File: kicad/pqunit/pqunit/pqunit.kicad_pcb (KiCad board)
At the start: 2 copper layers, 42 x 42 mm, 15 parts, among them J1 Conn_02x10_PQSU, J2 Conn_01x10, U1 ATMEGA328P-AU, U5 MAX485E, U6 Ai-Thinker-Ra-02, Y1 Crystal

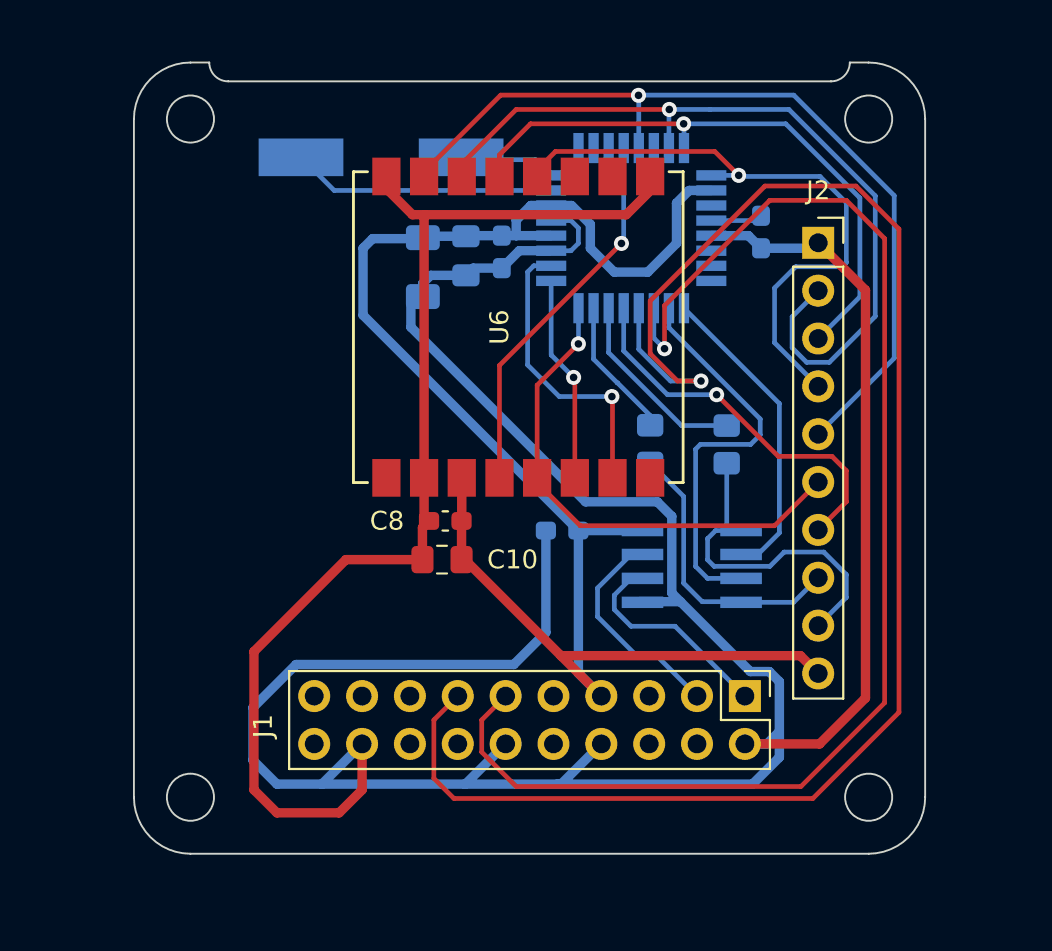
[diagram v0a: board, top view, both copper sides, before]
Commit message: Began PQUnit PCB Rev 2
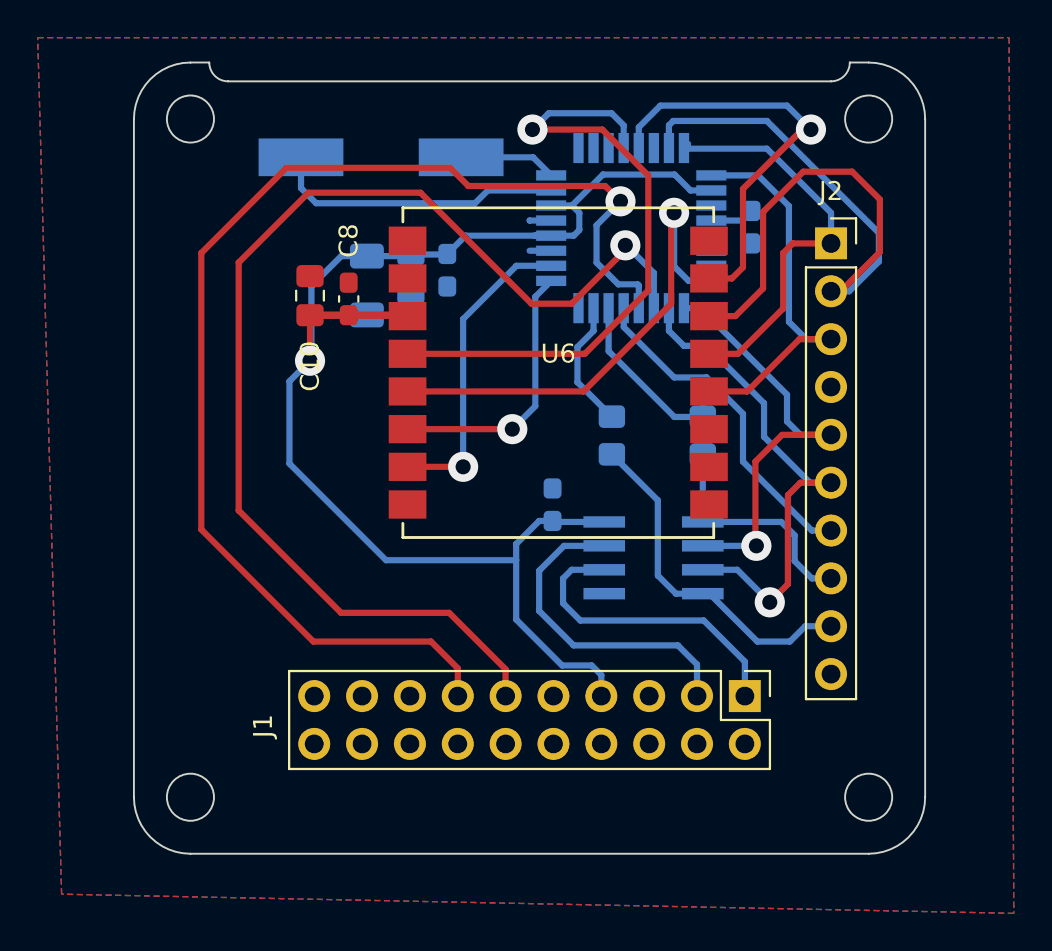
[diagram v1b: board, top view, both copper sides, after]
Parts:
- moved C10 15.7 mm to (131.3, 103.1), turned to 90 degrees
- moved C8 12.9 mm to (133.3, 103.3), turned to 90 degrees
- moved U6 3.21 mm to (144.4, 107.2), turned to 0 degrees
- moved C2 3.13 mm to (134.3, 102.6)
- moved C1 3.08 mm to (136.6, 102.0)
- moved C5 3.05 mm to (138.6, 101.8)
- moved R4 2.08 mm to (147.3, 110.6)
- moved U5 2.08 mm to (149.5, 117.1)
- moved C9 1.46 mm to (144.1, 114.2), turned to 90 degrees
- moved R3 1.35 mm to (152.1, 110.6)
- moved J2 0.68 mm to (158.9, 100.4)
- moved C4 0.56 mm to (154.7, 99.5)
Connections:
- J2 pad 1: GND -> SPI_MISO
- J2 pad 10: +3V3 -> GND
- J2 pad 3: SPI_MISO -> SPI_SCK
- J2 pad 4: SPI_SCK -> GND
- J2 pad 5: RF_NSS -> RS485_NRE
- J2 pad 6: RF_DIO0 -> RS485_DE
- J2 pad 8: MCU_TX -> MCU_RX
- J2 pad 9: MCU_RX -> MCU_TX
- U1 pad 24: unconnected-(U1-PC1(ADC1)-Pad24) -> RF_DIO0
- U1 pad 32: RF_DIO0 -> unconnected-(U1-PD2(INT0)-Pad32)
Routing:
- net GND: track 216.3 -> 2.30 mm
- net RF_NSS: track 46.3 -> 21.5 mm
- net I2C_SCL: track 86.5 -> 65.4 mm
- net +3V3: track 88.3 -> 74.2 mm, vias 0 -> 1
- net RF_NRESET: track 20.2 -> 34.1 mm
- net SPI_SCK: track 33.5 -> 21.8 mm, vias 1 -> 0
- net SPI_MISO: track 32.3 -> 21.8 mm, vias 1 -> 0
- net I2C_SDA: track 71.6 -> 62.2 mm
- net RS485_NRE: track 17.0 -> 23.4 mm, vias 0 -> 1
- net MCU_RX: track 18.4 -> 12.4 mm
- net RS485_SDB: track 11.5 -> 17.4 mm
- net RS485_DE: track 21.4 -> 27.1 mm, vias 0 -> 1
- net RS485_SDA: track 11.7 -> 16.5 mm
- net MCU_TX: track 14.7 -> 18.4 mm
- net RF_DIO1: track 11.0 -> 14.4 mm
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- added copper zone on B.Cu, net GND
- added copper zone on F.Cu, net GND

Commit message: Fixed all PQUnit PCB Rev 2 errors
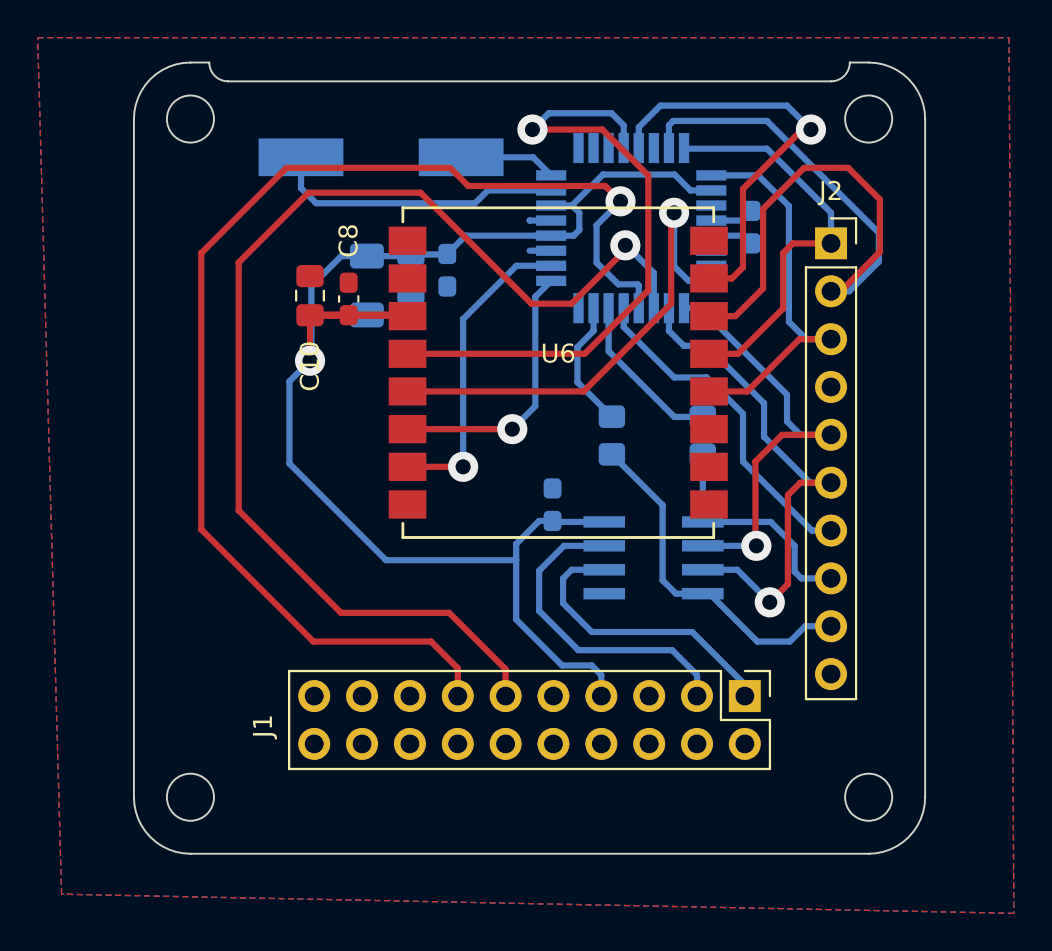
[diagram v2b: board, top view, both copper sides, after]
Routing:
- net GND: track 2.30 -> 4.61 mm
- net RS485_SDA: track 16.5 -> 15.7 mm
- net SPI_SCK: track 21.8 -> 21.2 mm
- net Net-(U1-PD0(RXD)): track 9.35 -> 8.73 mm

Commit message: Finished both PCB latest revisions
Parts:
- added JP1: Jumper_2_Bridged, TestPoint:TestPoint_2Pads_Pitch2.54mm_Drill0.8mm, F.Cu at (139.2, 117.5)
- C1, C10: footprint Capacitor_SMD:C_0805_2012Metric_Pad1.18x1.45mm_HandSolder -> Capacitor_SMD:C_1206_3216Metric_Pad1.33x1.80mm_HandSolder
- C4, C5, C8, C9: footprint Capacitor_SMD:C_0603_1608Metric_Pad1.08x0.95mm_HandSolder -> Capacitor_SMD:C_0805_2012Metric_Pad1.18x1.45mm_HandSolder
- moved C1 0.77 mm to (136.0, 102.5)
- moved C2 0.68 mm to (133.6, 102.4)
- moved C10 0.59 mm to (131.3, 102.5)
- moved C5 0.36 mm to (138.2, 101.9)
- moved C8 0.27 mm to (133.5, 103.1)
- moved C4 0.18 mm to (154.7, 99.7)
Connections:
- J1 pad 7: +3V3 -> 3V3_Bus
- J2 pad 4: GND -> RS485_NRE
- J2 pad 5: RS485_NRE -> RS485_DE
- J2 pad 6: RS485_DE -> MCU_NRESET
- J2 pad 7: MCU_NRESET -> MCU_RX
- J2 pad 8: MCU_RX -> MCU_TX
- J2 pad 9: MCU_TX -> +3V3
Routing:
- net +3V3: track 74.1 -> 84.3 mm
- net 3V3_Bus: track 0.00 -> 8.36 mm
- net RS485_DE: track 27.1 -> 24.4 mm
- net MCU_NRESET: track 18.0 -> 15.4 mm
- net MCU_TX: track 18.4 -> 17.4 mm
- net RS485_NRE: track 23.4 -> 22.6 mm
- net MCU_RX: track 12.4 -> 11.7 mm

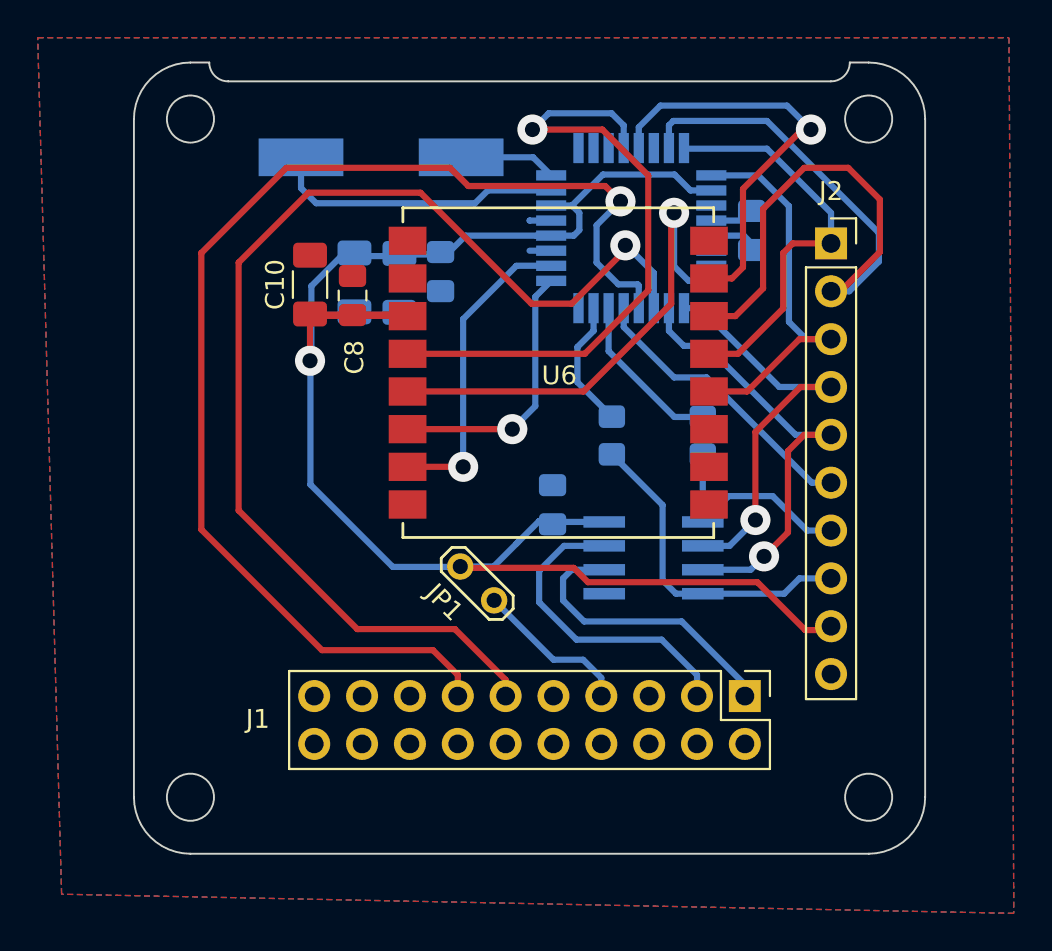
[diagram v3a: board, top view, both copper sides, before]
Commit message: Updated PQ PCB to include GPS and added initial PIO code
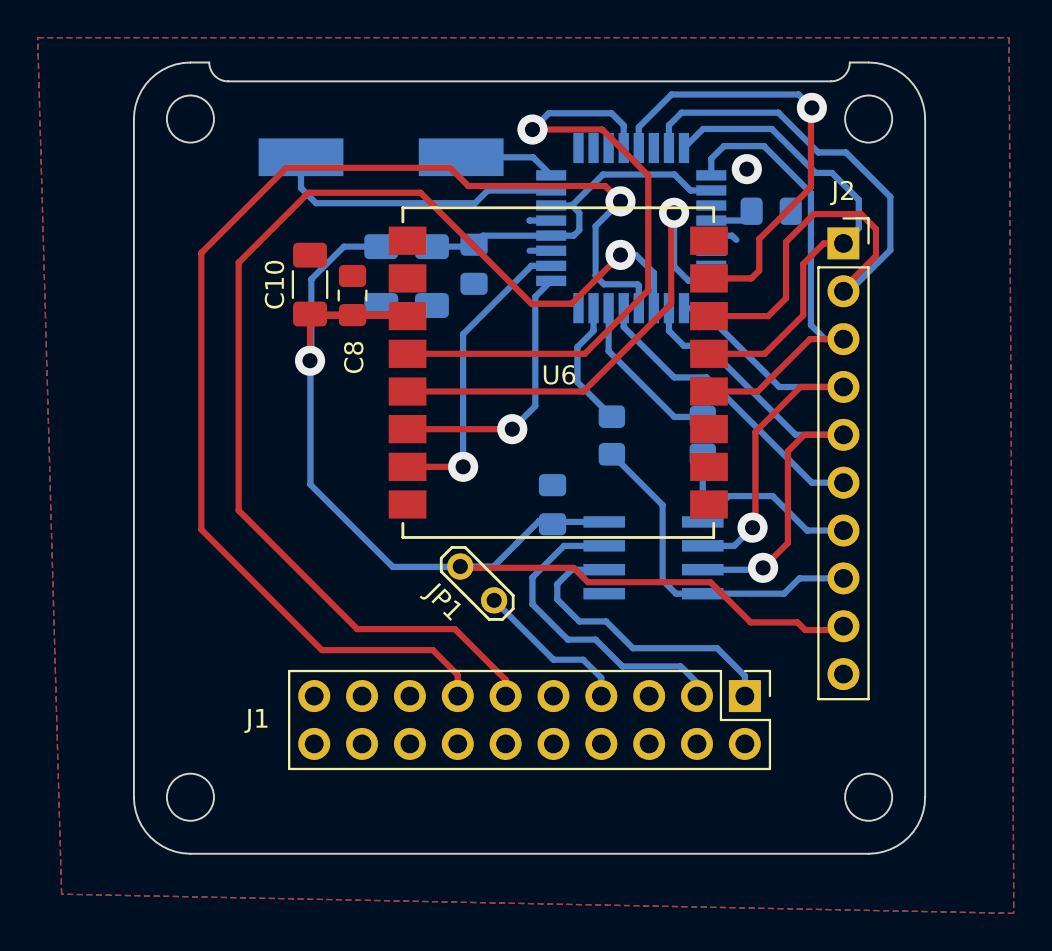
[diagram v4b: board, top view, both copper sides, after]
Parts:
- moved C5 1.82 mm to (140.0, 101.5)
- moved C1 1.76 mm to (137.7, 102.1)
- moved C2 1.46 mm to (135.0, 102.1)
- moved C4 1.46 mm to (155.7, 98.7), turned to 0 degrees
- moved J2 0.66 mm to (159.6, 100.4)
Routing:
- net SPI_SCK: track 21.2 -> 24.8 mm
- net SPI_MISO: track 21.5 -> 25.1 mm
- net SPI_MOSI: track 41.4 -> 38.5 mm
- net RS485_DE: track 24.4 -> 26.0 mm
- net RF_NSS: track 21.5 -> 23.1 mm
- net RS485_NRE: track 22.6 -> 24.0 mm
- net GND: track 4.61 -> 3.72 mm, vias 0 -> 1
- net +3V3: track 84.3 -> 85.1 mm
- net RS485_SDA: track 15.7 -> 16.3 mm
- net MCU_TX: track 17.4 -> 18.0 mm
- net MCU_RX: track 11.7 -> 12.4 mm
- net MCU_NRESET: track 15.4 -> 16.1 mm
- net I2C_SDA: track 61.8 -> 61.3 mm

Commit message: Added ISP
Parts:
- removed JP1: Jumper_2_Bridged, TestPoint:TestPoint_2Pads_Pitch2.54mm_Drill0.8mm
- added C6: 10uF, Capacitor_SMD:C_1206_3216Metric_Pad1.33x1.80mm_HandSolder, F.Cu at (131.7, 101.3)
- added J3: Conn_Coaxial, Connector_Coaxial:U.FL_Molex_MCRF_73412-0110_Vertical, F.Cu at (126.6, 124.6)
- added U3: ATGM332D-5N31, LIB_ATGM332D-5N31:ATGM332D5N31, F.Cu at (130.7, 113.8)
- Y1: moved to F.Cu
- moved U2 3.69 mm to (148.1, 107.4)
- moved C8 3.38 mm to (136.7, 101.9)
- moved C10 3.23 mm to (134.3, 101.3)
- moved R3 2.06 mm to (150.1, 110.5)
- moved C2 1.85 mm to (135.4, 100.3)
- moved C1 1.82 mm to (137.8, 100.3)
- moved C5 1.80 mm to (140.0, 99.7)
- moved J2 1.50 mm to (161.1, 100.4)
- moved C9 1.41 mm to (143.0, 115.1), turned to 180 degrees
- moved Y1 1.37 mm to (136.3, 95.3)
- renumbered U6 to U2, U5 to U4
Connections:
- J1 pad 7: 3V3_Bus -> +3V3
- J2 pad 9: +3V3 -> GND
- U1 pad 10: unconnected-(U1-PD6(AIN0)-Pad10) -> GPS_RX
- U1 pad 11: unconnected-(U1-PD7(AIN0)-Pad11) -> GPS_TX
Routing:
- net GPS_TX: track 0.00 -> 44.3 mm, vias 0 -> 1
- net GPS_RX: track 0.00 -> 39.0 mm, vias 0 -> 1
- net RF_NRESET: track 34.1 -> 22.8 mm
- net 3V3_Bus: track 8.36 -> 0.00 mm
- net Net-(J3-In): track 0.00 -> 5.05 mm
- net RS485_DE: track 26.0 -> 30.7 mm
- net +3V3: track 85.1 -> 80.9 mm
- net RS485_NRE: track 24.0 -> 27.8 mm
- net RF_DIO0: track 25.9 -> 22.4 mm
- net GND: track 3.72 -> 6.96 mm, vias 1 -> 2
- net RF_DIO1: track 14.3 -> 11.5 mm
- net MCU_TX: track 18.0 -> 20.8 mm
- net Net-(U1-PB6(XTAL1/TOSC1)): track 15.5 -> 12.9 mm, vias 0 -> 1
- net RF_NSS: track 23.1 -> 20.8 mm
- net RF_DIO2: track 16.2 -> 14.1 mm
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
